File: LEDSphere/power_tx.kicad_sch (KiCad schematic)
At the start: 88 parts, among them J1 USB_C_Receptacle_USB2.0, M1 Motor_DC, Q1 BSS138, Q2 BSS138, Q3 BSS138, Q4 BSS138, Q5 BSS138, Q6 BSS138, Q7 Si2319CDS, Q8 Si2319CDS, U1 4017, U10 Pin-Connector, U2 CH221K, U3 TPS54302, U4 SG3525, U8 UCC27714DR, U9 Pin-Connector

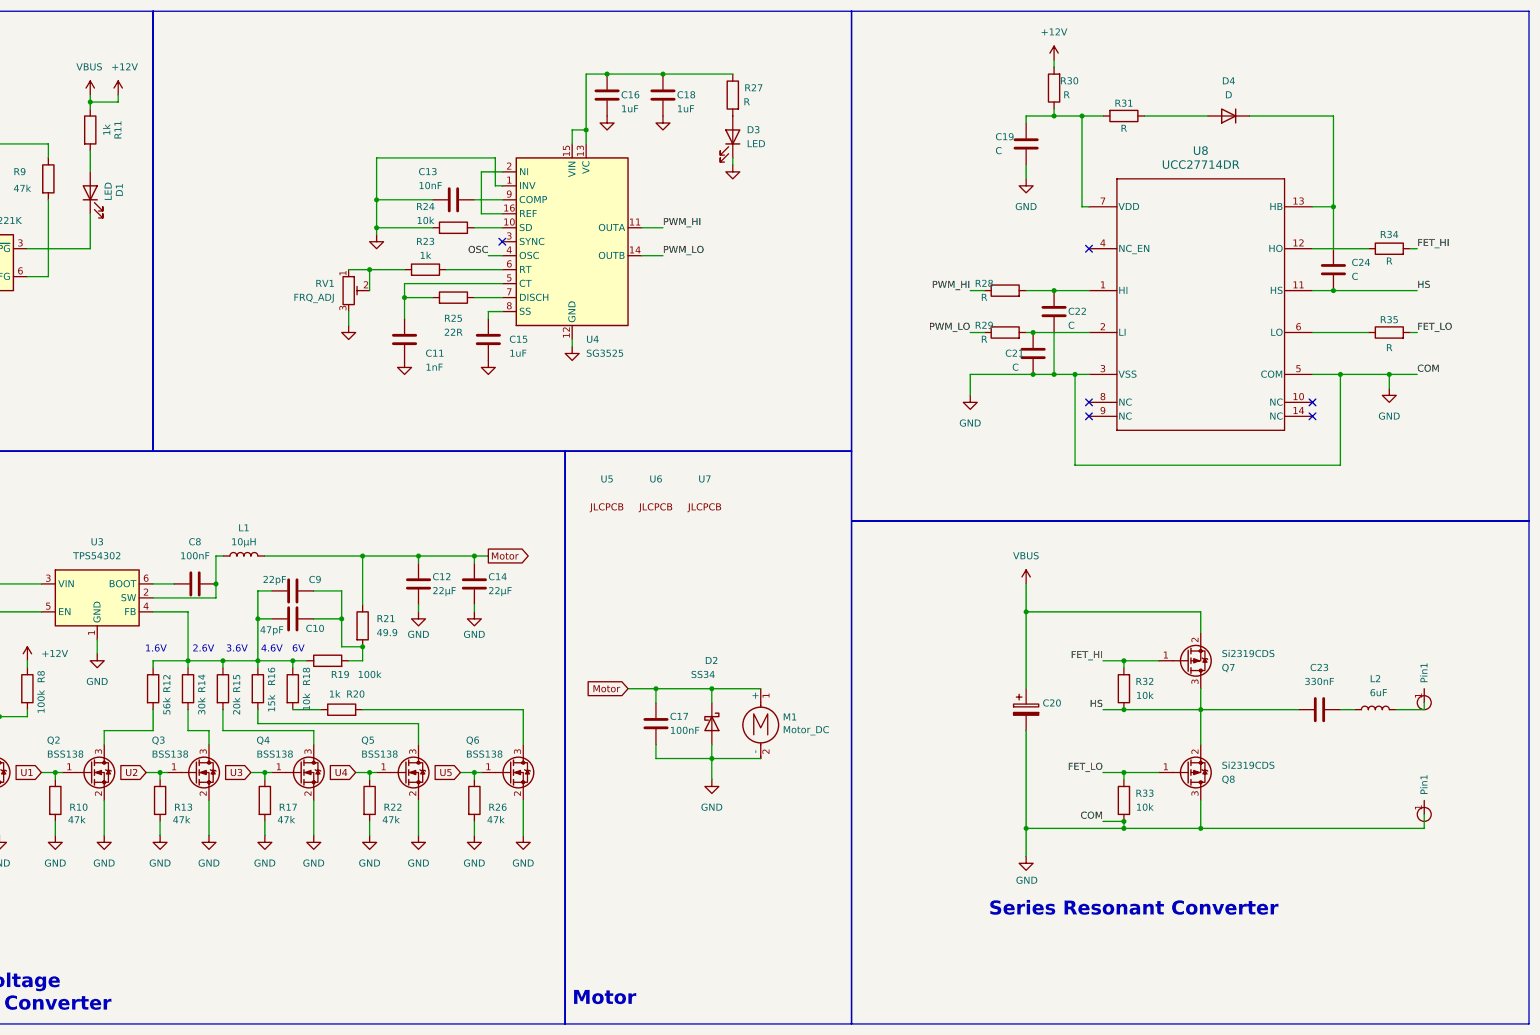
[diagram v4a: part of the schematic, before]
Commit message: Add Initial Schematic for Review
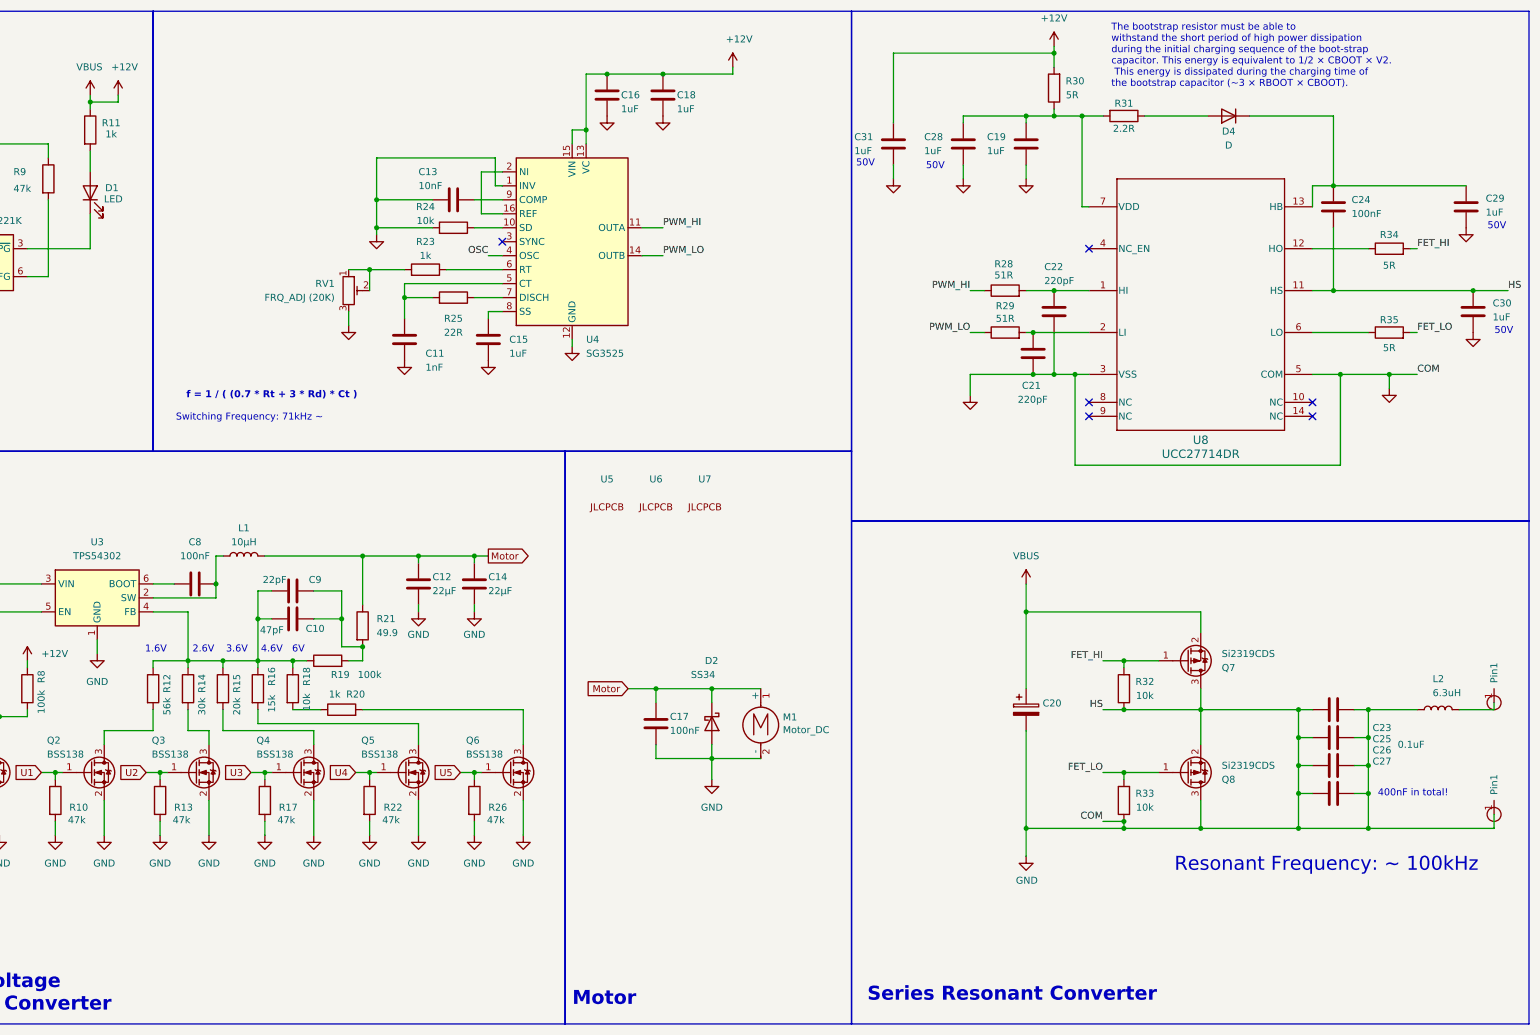
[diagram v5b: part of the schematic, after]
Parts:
- removed D3: LED, symbol Device:LED
- removed R27: R, symbol Device:R
- added C25, C26, C27: 100nF, Capacitor_SMD:C_0603_1608Metric, symbol Device:C
- added C28, C29, C30: 1uF, Capacitor_SMD:C_0805_2012Metric, symbol Device:C
- added C31: 1uF, Capacitor_THT:C_Radial_D8.0mm_H7.0mm_P3.50mm, symbol Device:C
- C11, C13: footprint (none) -> Capacitor_SMD:C_0603_1608Metric
- C15: footprint (none) -> Capacitor_SMD:C_0402_1005Metric
- C16, C18: footprint (none) -> Capacitor_SMD:C_0805_2012Metric
- C19: value C -> 1uF; footprint (none) -> Capacitor_SMD:C_0603_1608Metric
- C21, C22: value C -> 220pF; footprint (none) -> Capacitor_SMD:C_0402_1005Metric
- C23: value 330nF -> 0.1uF; footprint (none) -> Capacitor_SMD:C_0603_1608Metric; LCSC (none) -> C14663
- C24: value C -> 100nF; footprint (none) -> Capacitor_SMD:C_0603_1608Metric
- D2: footprint my_footprints:DIOM7959X265N -> LEDSphere_Footprints:DIOM7959X262N
- D4: footprint (none) -> Diode_SMD:D_SMA
- J1: footprint my_footprints:USB_C_Receptacle -> Connector_USB:USB_C_Receptacle_GCT_USB4105-xx-A_16P_TopMnt_Horizontal
- L2: value 6uF -> 6.3uH
- M1: footprint my_footprints:motor -> LEDSphere_Footprints:motor
- R23, R24, R25: footprint (none) -> Resistor_SMD:R_0402_1005Metric
- R28, R29: value R -> 51R; footprint (none) -> Resistor_SMD:R_0603_1608Metric
- R30, R34, R35: value R -> 5R; footprint (none) -> Resistor_SMD:R_0603_1608Metric
- R31: value R -> 2.2R; footprint (none) -> Resistor_SMD:R_0603_1608Metric
- R32, R33: footprint (none) -> Resistor_SMD:R_0603_1608Metric
- RV1: value FRQ_ADJ -> FRQ_ADJ (20K); footprint (none) -> LEDSphere_Footprints:TRIM_3362P-1-203LF
- SW1, SW2: footprint my_footprints:XKB5858-X-F-75 -> LEDSphere_Footprints:XKB5858-X-F-75
- U1: footprint Package_SO:SOP-16_3.9x9.9mm_P1.27mm -> Package_SO:STC_SOP-16_3.9x9.9mm_P1.27mm
- U4: footprint (none) -> LEDSphere_Footprints:SO-16N_STM
- U8: footprint D0014A_N -> LEDSphere_Footprints:D0014A
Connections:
- net HS is gone; now on net GND: C23.1, C24.2, Q7.3 (D), Q8.2 (S), R32.1, U8.11 (HS)
- net +12V: now also C16.1, C18.1, U4.13 (VC), U4.15 (VIN), C31.1
- net GND: now also C23.2, L2.1, C25.1, C25.2, C26.1, C26.2, C27.1, C27.2, C28.2, C29.2, C30.1, C30.2, C31.2
- net at C19.1, R30.1, R31.2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: now also C28.1
- net at C24.1, D4.1 (K), U8.13 (HB): now also C29.1
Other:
- note added: "400nF in total!"
- note added: "50V"
- note added: "Resonant Frequency: ~ 100kHz"
- note added: "Switching Frequency: 71kHz ~"
- note added: "The bootstrap resistor must be able to withstand the short period of high power dissipation during the initial charging sequence of the boot-strap capacitor. This energy is equivalent to 1/2 × CBOOT × V2. This energy is dissipated during the charging time of the bootstrap capacitor (~3 × RBOOT × CBOOT)."
- note added: "f = 1 / ( (0.7 * Rt + 3 * Rd) * Ct )"
- moved on the sheet: C24, L2

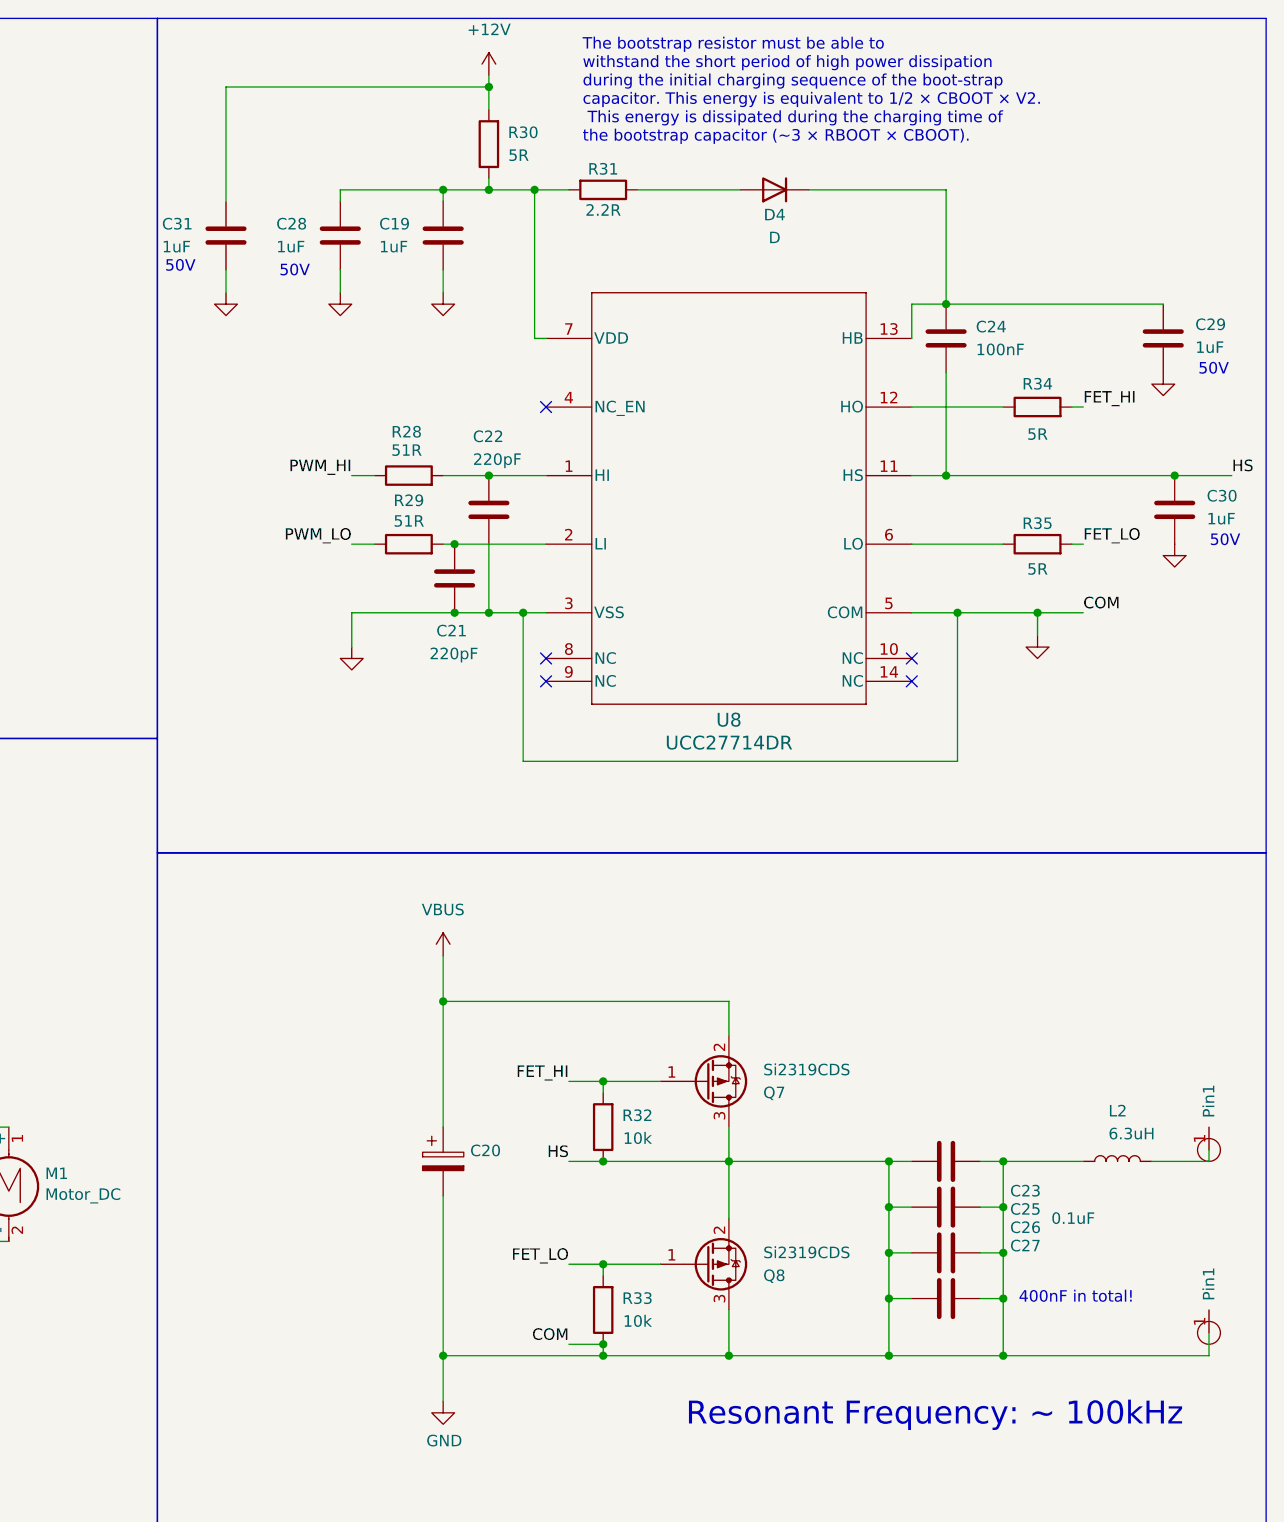
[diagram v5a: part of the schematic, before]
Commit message: Add PCB Coil for Transmitter
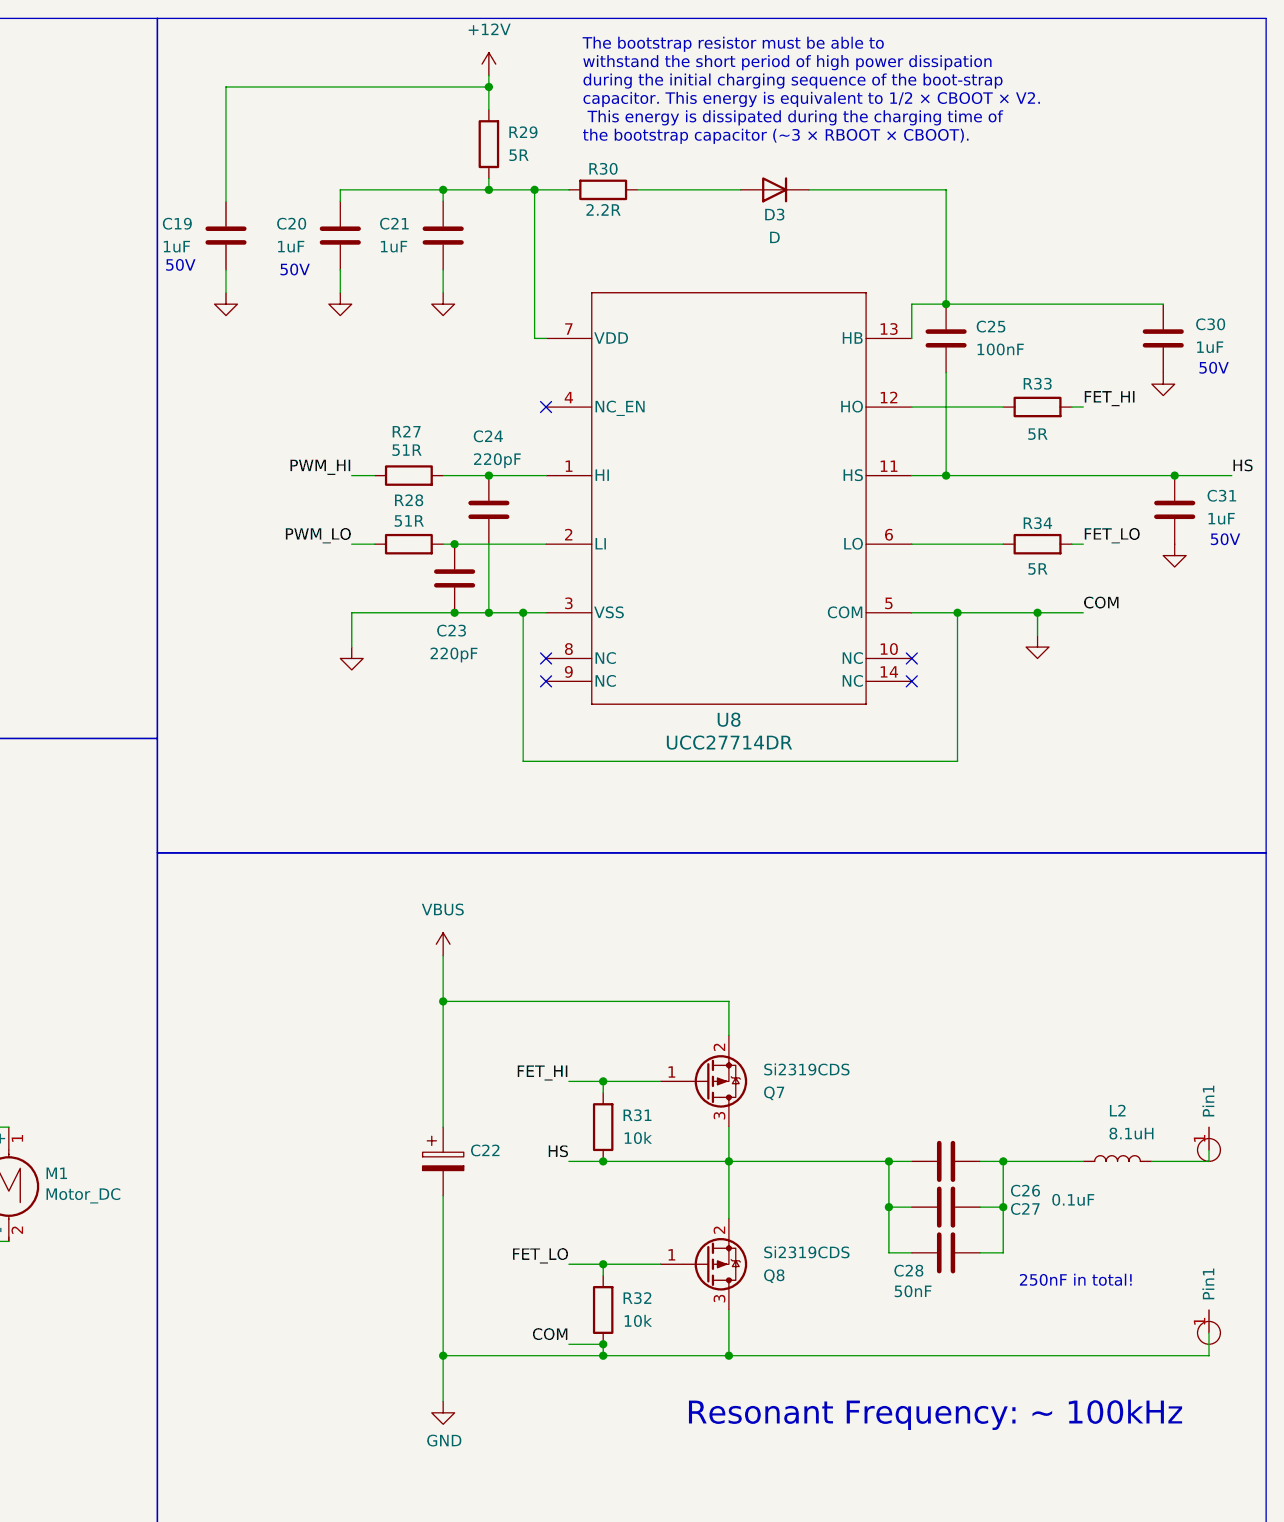
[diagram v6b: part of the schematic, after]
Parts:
- removed C27: 100nF, Capacitor_SMD:C_0603_1608Metric, symbol Device:C
- C28: renamed from C26; value 100nF -> 50nF
- L2: value 6.3uH -> 8.1uH
- renumbered C31 to C19, C28 to C20, C19 to C21, C20 to C22, C21 to C23, C22 to C24, C24 to C25, C23 to C26, C25 to C27, C29 to C30, C30 to C31, D4 to D3, R28 to R27, R29 to R28, R30 to R29, R31 to R30, R32 to R31, R33 to R32, R34 to R33, R35 to R34
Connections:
- net GND: no longer C25.2, C26.1, C26.2, C27.1, C27.2, C28.1, C28.2, C31.1, L2.1, Q7.3 (D), Q8.2 (S), R31.1, U8.11 (HS)
- new net: C26.2, C27.2, C28.2, L2.1
- new net HS: C25.2, C26.1, C27.1, C28.1, C31.1, Q7.3 (D), Q8.2 (S), R31.1, U8.11 (HS)
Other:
- note added: "250nF in total!"
- note removed: "400nF in total!"

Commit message: Starting Layout
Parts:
- D2: footprint LEDSphere_Footprints:DIOM7959X262N -> Footprints:DIOM7959X262N
- M1: footprint LEDSphere_Footprints:motor -> Footprints:motor
- RV1: footprint LEDSphere_Footprints:TRIM_3362P-1-203LF -> Footprints:TRIM_3362P-1-203LF
- SW1, SW2: footprint LEDSphere_Footprints:XKB5858-X-F-75 -> Footprints:XKB5858-X-F-75
- U4: footprint LEDSphere_Footprints:SO-16N_STM -> Footprints:SO-16N_STM
- U8: footprint LEDSphere_Footprints:D0014A -> Footprints:D0014A
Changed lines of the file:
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@@
 			)
 		)
-		(property "Footprint" "LEDSphere_Footprints:DIOM7959X262N"
+		(property "Footprint" "Footprints:DIOM7959X262N"
 			(at 259.08 142.24 0)
 			(hide yes)
@@
 			)
 		)
-		(property "Footprint" "LEDSphere_Footprints:TRIM_3362P-1-203LF"
+		(property "Footprint" "Footprints:TRIM_3362P-1-203LF"
 			(at 193.04 63.5 0)
 			(hide yes)
@@
 			)
 		)
-		(property "Footprint" "LEDSphere_Footprints:XKB5858-X-F-75"
+		(property "Footprint" "Footprints:XKB5858-X-F-75"
 			(at 29.21 142.24 0)
 			(hide yes)
@@
 			)
 		)
-		(property "Footprint" "LEDSphere_Footprints:motor"
+		(property "Footprint" "Footprints:motor"
 			(at 267.97 143.256 0)
 			(hide yes)
@@
 			)
 		)
-		(property "Footprint" "LEDSphere_Footprints:D0014A"
+		(property "Footprint" "Footprints:D0014A"
 			(at 347.98 66.04 0)
 			(hide yes)
@@
 			)
 		)
-		(property "Footprint" "LEDSphere_Footprints:XKB5858-X-F-75"
+		(property "Footprint" "Footprints:XKB5858-X-F-75"
 			(at 53.34 142.24 0)
 			(hide yes)
@@
 			)
 		)
-		(property "Footprint" "LEDSphere_Footprints:SO-16N_STM"
+		(property "Footprint" "Footprints:SO-16N_STM"
 			(at 233.68 54.61 0)
 			(hide yes)

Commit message: Initial Layout (Rounded Tracks)
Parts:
- removed U10, U9: Pin-Connector, my_footprints:Pin_2mm, symbol my_symbols:Pin-Connector
- removed U5, U6, U7: (no value), my_footprints:JLC_tooling_hole, symbol New_Library:JLCPCB
- C19: footprint Capacitor_THT:C_Radial_D8.0mm_H7.0mm_P3.50mm -> Capacitor_SMD:C_1206_3216Metric
- L2: footprint (none) -> Footprints:power_coil
- R11: value 1k -> 10k
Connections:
- net +5V is gone; now on net +12V: C3.1
- net GND: now also L2.2
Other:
- moved on the sheet: C22, C26, C27, C28, D2, Q7, Q8, R31, R32
